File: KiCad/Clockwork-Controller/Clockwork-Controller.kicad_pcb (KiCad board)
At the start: 2 copper layers, 56.4 x 94.2 mm, 97 parts, among them CN2 PJ-307N5, J2 to DIN-6 Male, J3 Pause Button, J4 ICSP, J5 LED-Connector, Q1 AO3400A, Q2 SS8050, Q3 SS8050, Q4 SS8050, SW1 Guide/Follow, SW2 Mode -, SW3 Mode +, SW4 Frame -, SW5 Frame +, U1 ECS-TXO-3225MV-160-TR, U2 AP2210N-3.3TRG1, U3 74HCT14, U4 G3VM-61VY3(TR), U5 MCP4725, U6 LMC6482, U7 ATmega328P-A

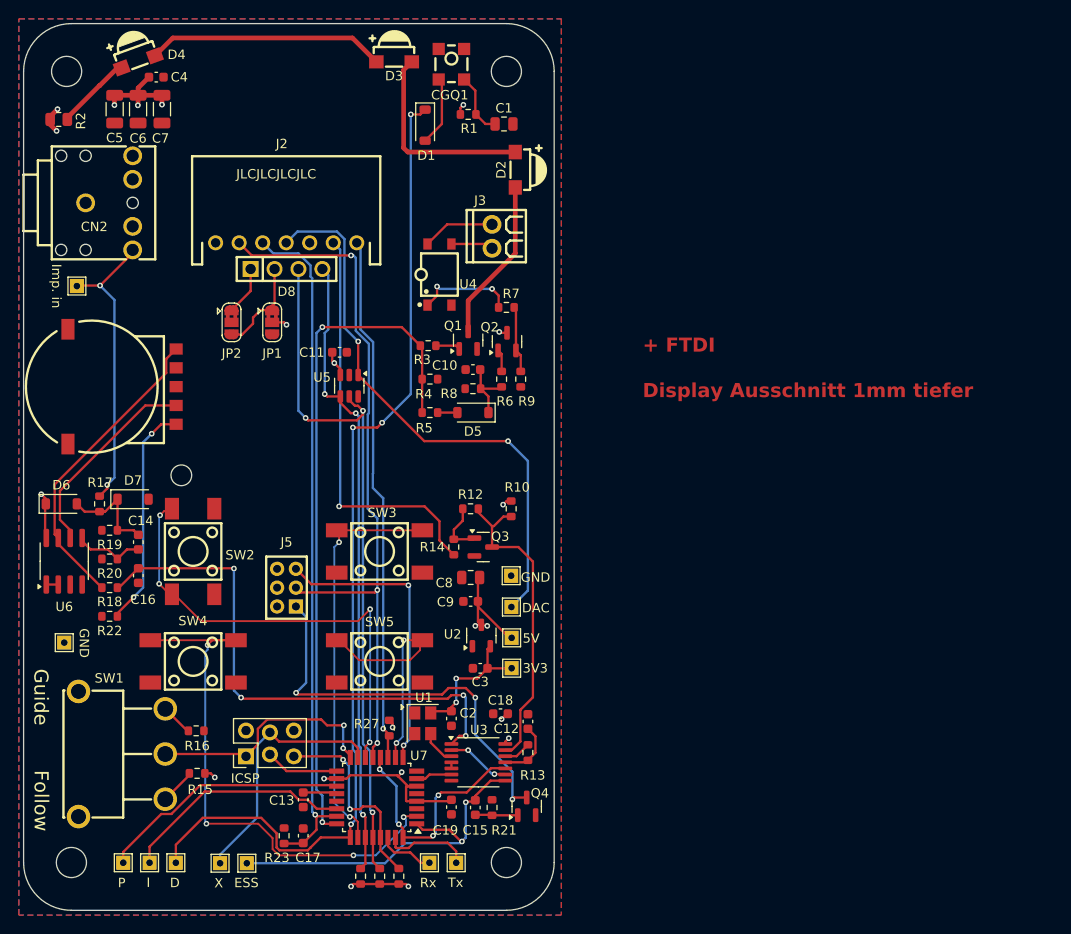
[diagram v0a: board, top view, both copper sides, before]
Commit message: Adding FTDI port
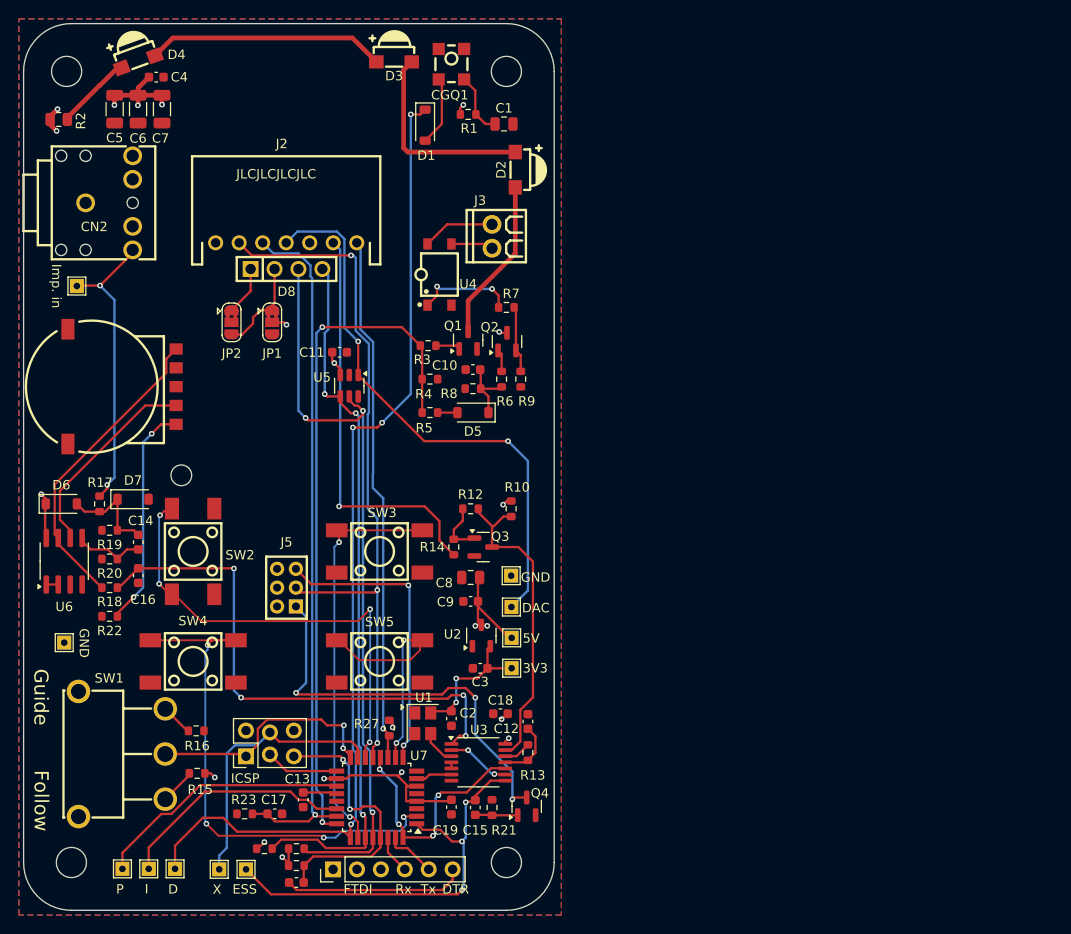
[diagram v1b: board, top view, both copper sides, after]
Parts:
- removed TP12: Rx, TestPoint:TestPoint_THTPad_1.5x1.5mm_Drill0.7mm
- removed TP13: Tx, TestPoint:TestPoint_THTPad_1.5x1.5mm_Drill0.7mm
- added C20: 100n, Capacitor_SMD:C_0603_1608Metric, F.Cu at (67.6, 111.6)
- added J6: FTDI, Connector_PinHeader_2.54mm:PinHeader_1x06_P2.54mm_Vertical, F.Cu at (71.5, 110.2)
- moved R26 10.9 mm to (67.6, 109.8), turned to 0 degrees
- moved R24 10.6 mm to (64.2, 108.0), turned to 180 degrees
- moved R25 9.33 mm to (67.6, 108.0), turned to 0 degrees
- moved R23 4.80 mm to (62.1, 104.3), turned to 180 degrees
- moved C17 3.82 mm to (65.3, 104.3), turned to 0 degrees
- moved TP10 0.66 mm to (62.2, 110.2)
- moved TP6 0.66 mm to (49.1, 110.1)
- moved TP7 0.66 mm to (51.9, 110.1)
- moved TP8 0.66 mm to (59.4, 110.2)
- moved TP11 0.66 mm to (54.7, 110.1)
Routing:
- net /DTR: track 0.00 -> 19.3 mm
- net /SDA: track 67.2 -> 75.5 mm
- net /~{RST}: track 21.5 -> 29.2 mm
- net /INT1: track 39.4 -> 44.9 mm, vias 2 -> 3
- net /SCL: track 74.7 -> 79.9 mm
- net /TX: track 9.36 -> 5.55 mm
- net /Frame-: track 57.7 -> 55.5 mm
- net +5V: track 66.7 -> 64.4 mm
- net /MOSI: track 27.1 -> 29.2 mm
- net /RX: track 6.06 -> 4.13 mm
- net /Proj_ID: track 72.7 -> 74.5 mm
- net /D_POT: track 107.6 -> 106.3 mm
- net /I_POT: track 24.8 -> 25.5 mm
- net /P_POT: track 26.8 -> 27.5 mm
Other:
- board text added: "DTR"
- board text added: "FTDI"
- board text removed: "+ FTDI Display Ausschnitt 1mm tiefer"

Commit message: Label it Rev.B
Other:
- board text added: "Rev.B"
- board text removed: "Rev.A"
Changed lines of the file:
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@@
 		)
 	)
-	(gr_text "Rev.A"
+	(gr_text "Rev.B"
 		(at 71.628 79.756 90)
 		(layer "B.SilkS")

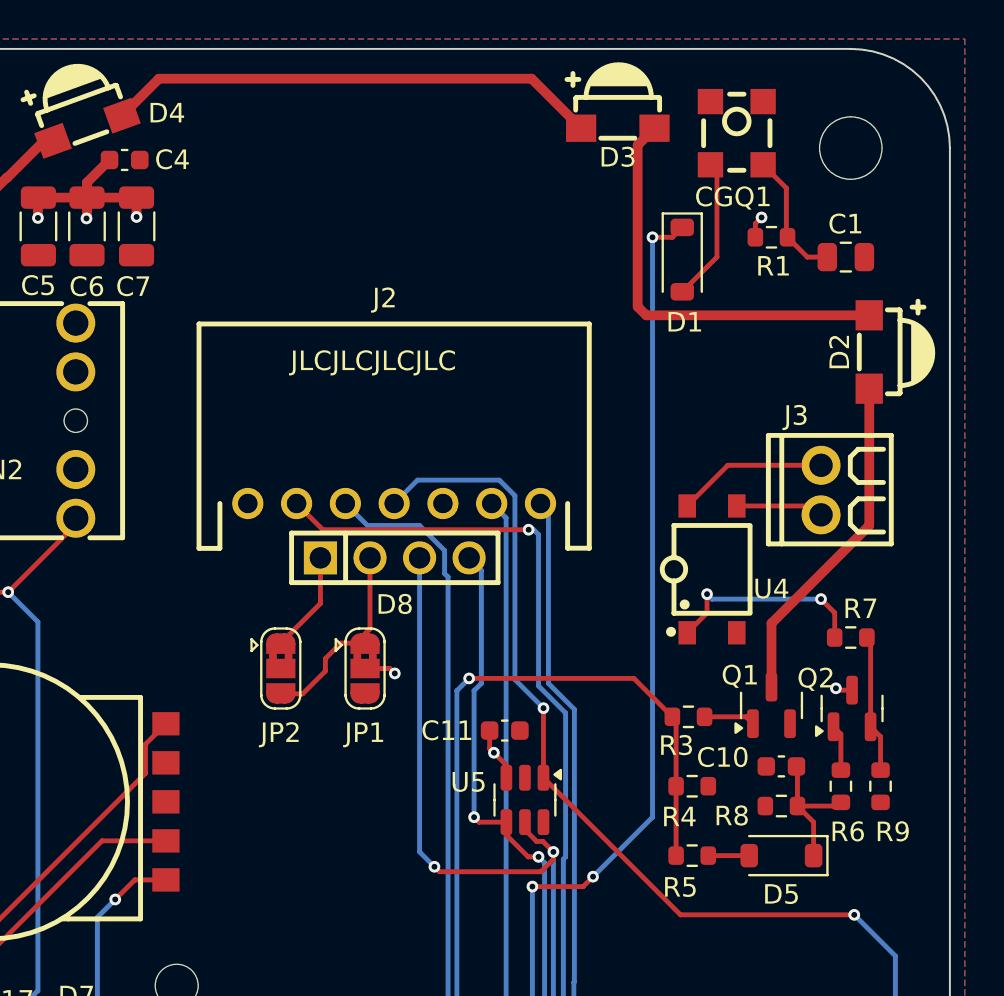
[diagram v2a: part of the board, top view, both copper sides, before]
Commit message: Swapping IR Tx and Rx for better reach
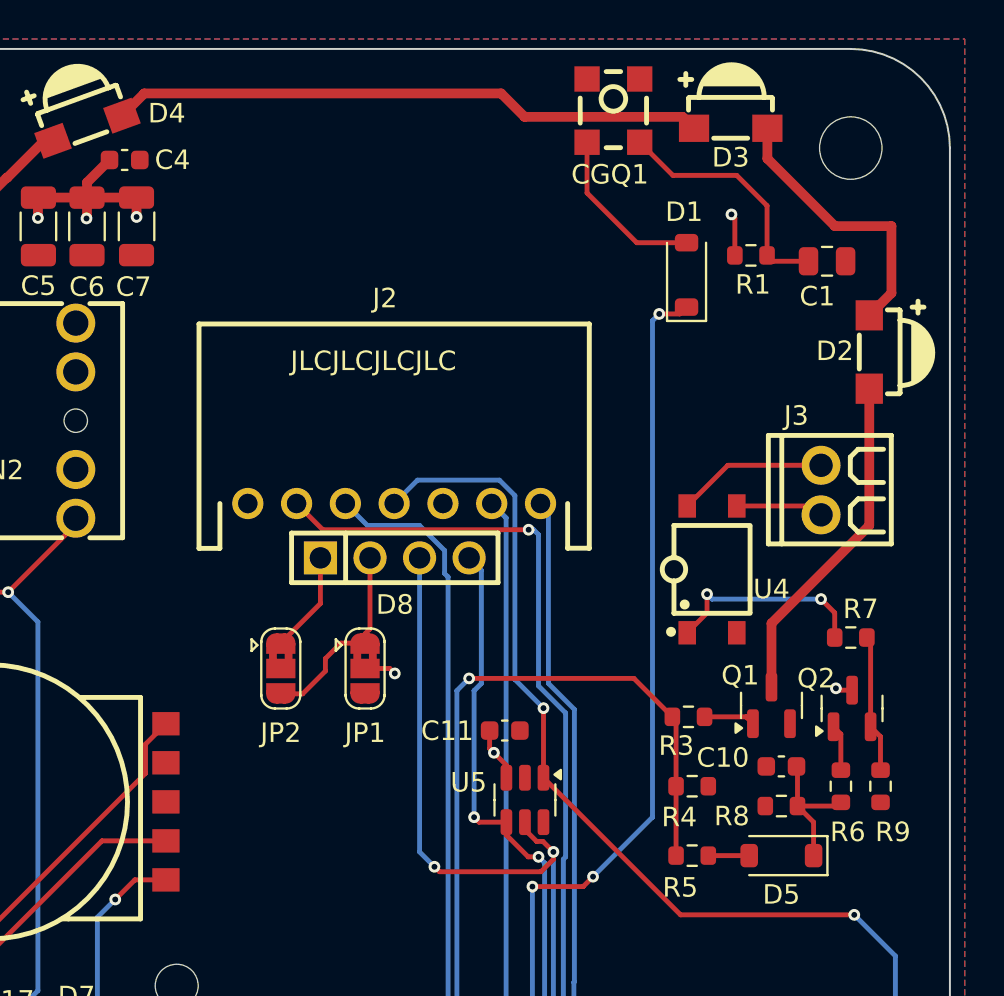
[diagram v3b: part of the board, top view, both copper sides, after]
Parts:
- moved CGQ1 6.43 mm to (77.8, 23.5)
- moved D3 5.78 mm to (83.8, 24.4)
- moved R1 1.40 mm to (84.8, 30.9)
- moved C1 0.99 mm to (88.7, 31.2)
- moved D1 0.82 mm to (81.5, 31.9), turned to 90 degrees
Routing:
- net Net-(D2-A): track 21.6 -> 14.4 mm
- net Net-(CGQ1-VCC): track 6.69 -> 12.7 mm
- net Net-(D3-A): track 25.4 -> 30.5 mm
- net /D_POT: track 106.3 -> 102.3 mm
- net Net-(CGQ1-VOUT): track 7.38 -> 8.76 mm
- net +5V: track 64.4 -> 65.5 mm

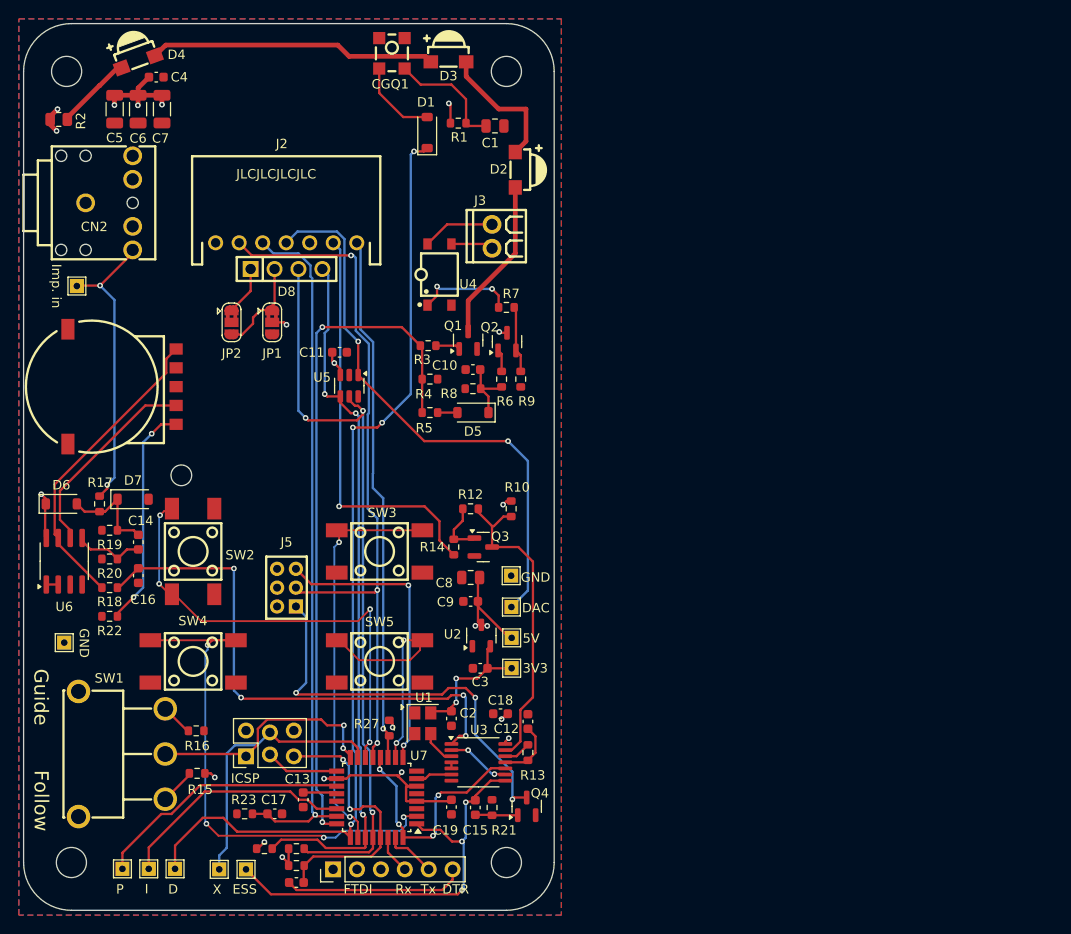
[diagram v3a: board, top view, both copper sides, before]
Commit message: Adjusting LED-Pins on the Controller Side (adding VCC)
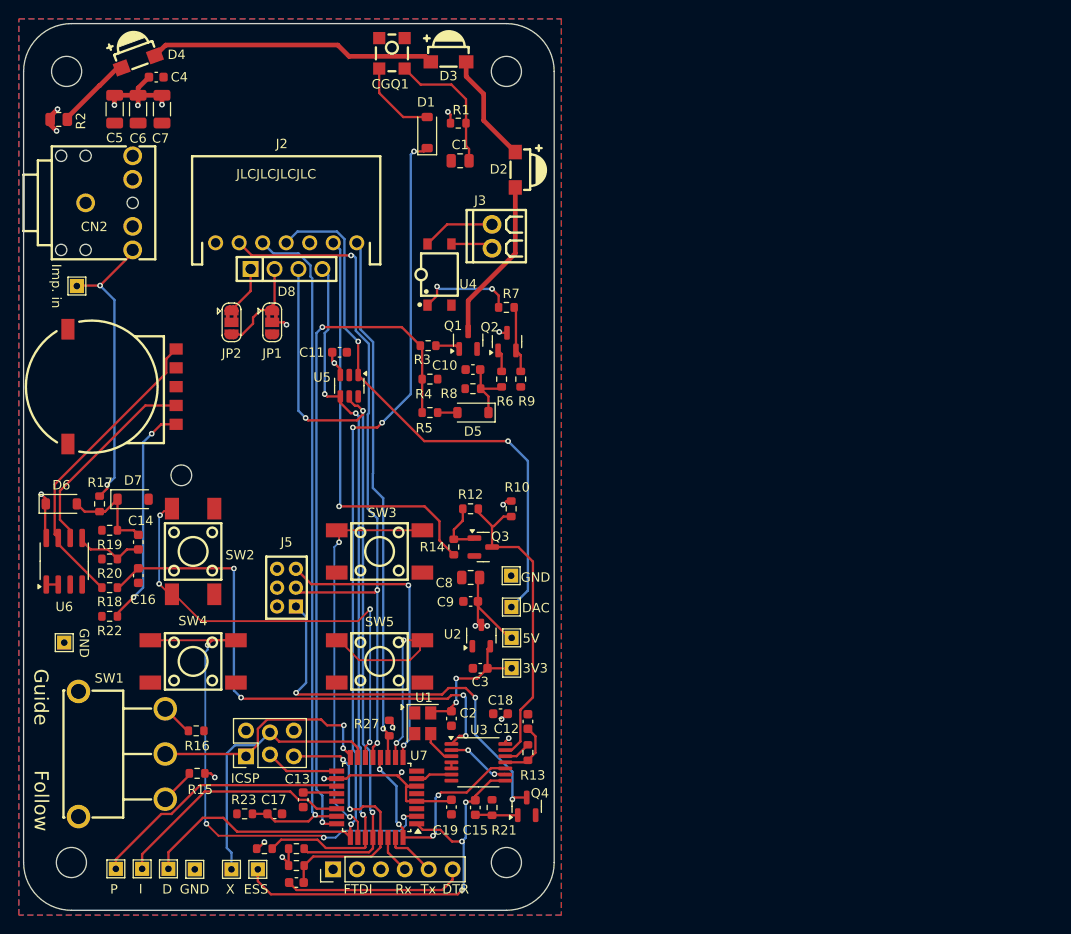
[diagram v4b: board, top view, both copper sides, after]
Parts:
- added TP12: GND, TestPoint:TestPoint_THTPad_1.5x1.5mm_Drill0.7mm, F.Cu at (56.8, 110.2)
- moved C1 5.23 mm to (85.0, 34.9), turned to 180 degrees
- moved TP8 1.30 mm to (60.7, 110.2)
- moved TP10 1.26 mm to (63.5, 110.2)
- moved TP11 0.70 mm to (54.0, 110.1)
- moved TP6 0.70 mm to (48.4, 110.1)
- moved TP7 0.70 mm to (51.2, 110.1)
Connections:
- net /In_Sync-LED renamed /No_Sync-LED
- J5 pad 2: GND -> +5V
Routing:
- net Net-(D2-A): track 14.4 -> 11.7 mm
- net Net-(CGQ1-VCC): track 12.7 -> 14.6 mm
- net +5V: track 65.5 -> 64.6 mm
- net /INT1: track 44.9 -> 44.4 mm

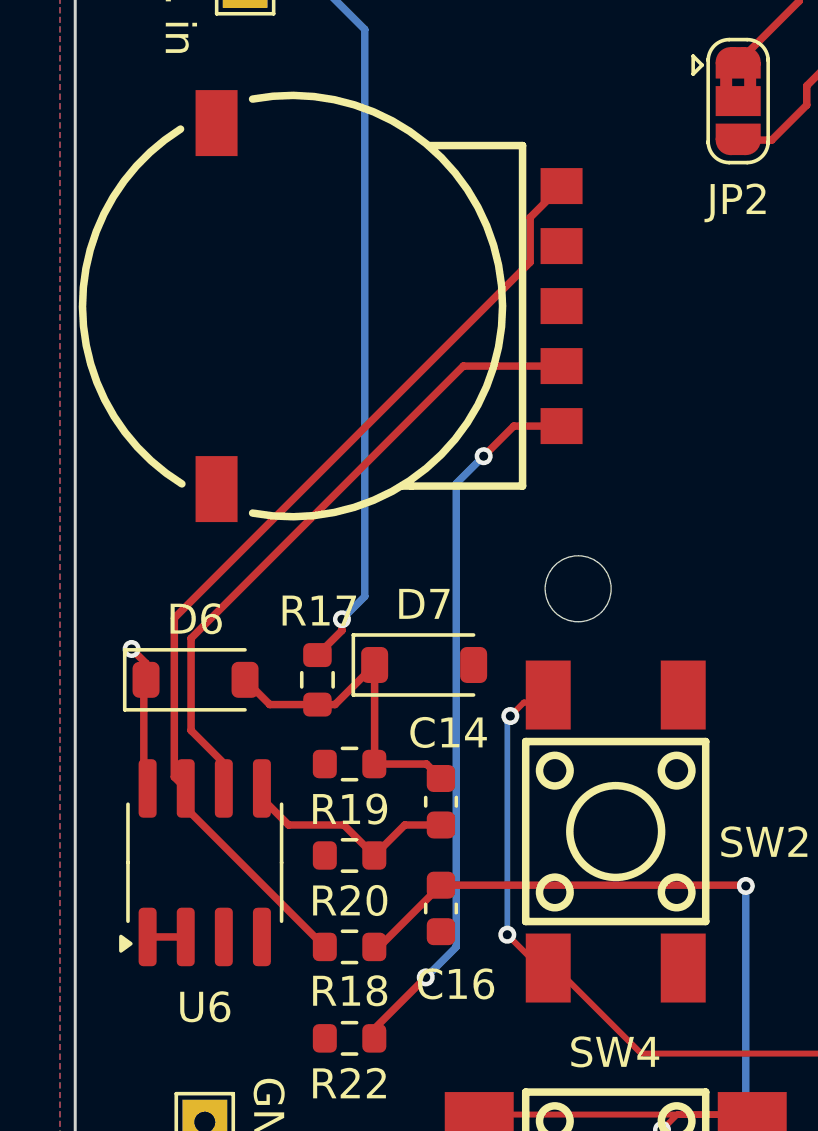
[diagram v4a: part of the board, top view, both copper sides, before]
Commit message: Potentiometer Flip for more intuitive Pulse Amp control
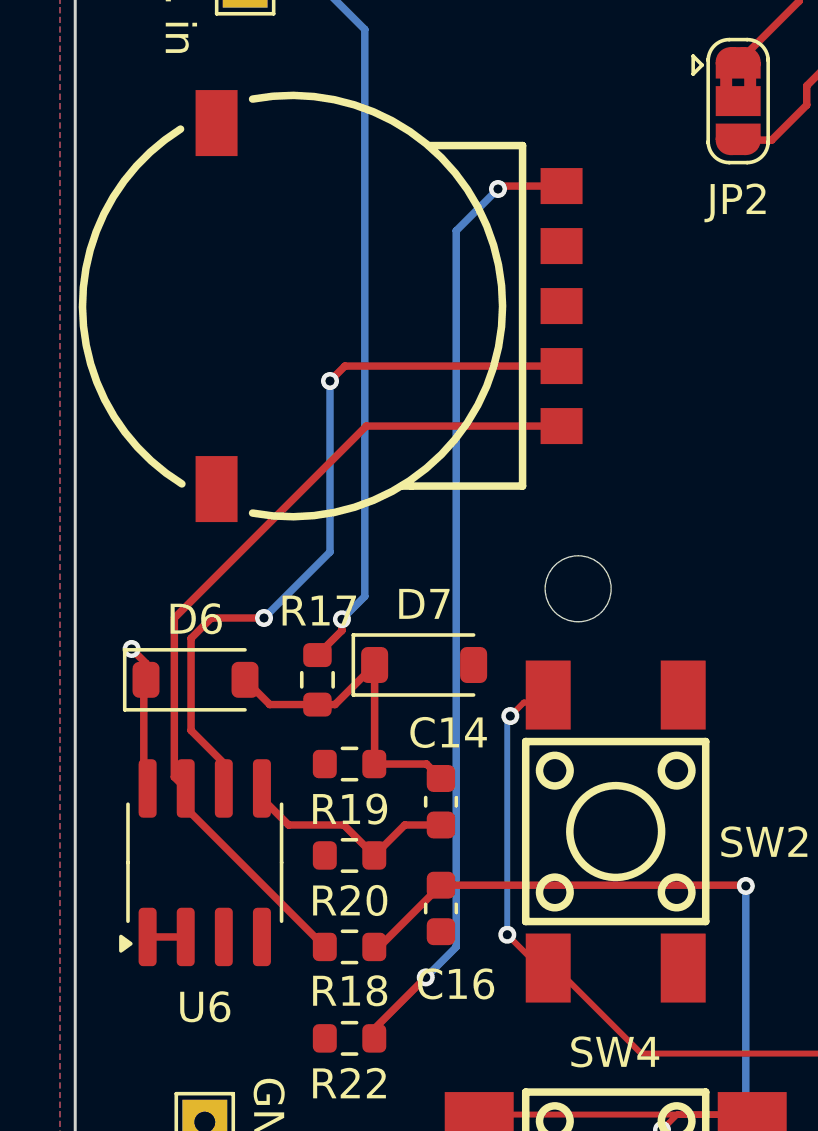
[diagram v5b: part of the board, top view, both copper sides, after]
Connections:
- RV1 pad 1: Net-(R22-Pad1) -> Net-(R18-Pad1)
- RV1 pad 3: Net-(R18-Pad1) -> Net-(R22-Pad1)
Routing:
- net Net-(R22-Pad1): track 23.9 -> 32.2 mm
- net Net-(R18-Pad1): track 32.8 -> 28.6 mm
- net Net-(U6B--): track 21.6 -> 24.9 mm, vias 0 -> 2
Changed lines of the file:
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@@
 			(size 1.4 1.2)
 			(layers "F.Cu" "F.Paste" "F.Mask")
-			(net 56 "Net-(R22-Pad1)")
+			(net 55 "Net-(R18-Pad1)")
 			(pinfunction "1")
 			(pintype "passive")
@@
 			(size 1.4 1.2)
 			(layers "F.Cu" "F.Paste" "F.Mask")
-			(net 55 "Net-(R18-Pad1)")
+			(net 56 "Net-(R22-Pad1)")
 			(pinfunction "3")
 			(pintype "passive")
@@
 	)
 	(segment
-		(start 53.7718 57.440922)
-		(end 53.7718 55.949932)
-		(width 0.25)
-		(layer "F.Cu")
-		(net 55)
-	)
-	(segment
 		(start 42.291 75.628)
 		(end 42.291 74.982)
@@
 	)
 	(segment
-		(start 53.7718 55.949932)
-		(end 54.819132 54.9026)
+		(start 41.91 69.302722)
+		(end 48.310122 62.9026)
 		(width 0.25)
 		(layer "F.Cu")
@@
 	)
 	(segment
-		(start 41.91 69.302722)
-		(end 53.7718 57.440922)
+		(start 48.310122 62.9026)
+		(end 54.819132 62.9026)
 		(width 0.25)
 		(layer "F.Cu")
@@
 	)
 	(segment
-		(start 52.2224 63.9064)
-		(end 53.2262 62.9026)
+		(start 54.819132 54.9026)
+		(end 52.7974 54.9026)
 		(width 0.25)
 		(layer "F.Cu")
@@
 	)
 	(segment
-		(start 50.292 81.28)
-		(end 48.577 82.995)
+		(start 52.7974 54.9026)
+		(end 52.7 55)
 		(width 0.25)
 		(layer "F.Cu")
@@
 	)
 	(segment
-		(start 53.2262 62.9026)
-		(end 54.819132 62.9026)
+		(start 50.292 81.28)
+		(end 48.577 82.995)
 		(width 0.25)
 		(layer "F.Cu")
@@
 	)
 	(via
-		(at 52.2224 63.9064)
+		(at 52.7 55)
 		(size 0.6)
 		(drill 0.3)
@@
 	)
 	(segment
-		(start 51.308 80.264)
-		(end 50.292 81.28)
+		(start 51.308 56.392)
+		(end 51.308 80.264)
 		(width 0.25)
 		(layer "B.Cu")
@@
 	)
 	(segment
-		(start 52.2224 63.9064)
-		(end 51.308 64.8208)
+		(start 52.7 55)
+		(end 51.308 56.392)
 		(width 0.25)
 		(layer "B.Cu")
@@
 	)
 	(segment
-		(start 51.308 64.8208)
-		(end 51.308 80.264)
+		(start 51.308 80.264)
+		(end 50.292 81.28)
 		(width 0.25)
 		(layer "B.Cu")
@@
 	)
 	(segment
-		(start 51.5432 60.9026)
-		(end 42.4688 69.977)
+		(start 44.9 69.3)
+		(end 43.1458 69.3)
 		(width 0.25)
 		(layer "F.Cu")
@@
 	(segment
 		(start 54.819132 60.9026)
-		(end 51.5432 60.9026)
+		(end 47.5974 60.9026)
+		(width 0.25)
+		(layer "F.Cu")
+		(net 57)
+	)
+	(segment
+		(start 47.5974 60.9026)
+		(end 47.1 61.4)
 		(width 0.25)
 		(layer "F.Cu")
@@
 	)
 	(segment
+		(start 43.1458 69.3)
+		(end 42.4688 69.977)
+		(width 0.25)
+		(layer "F.Cu")
+		(net 57)
+	)
+	(segment
 		(start 42.4688 69.977)
 		(end 42.4688 73.0504)
@@
 		(net 57)
 	)
+	(via
+		(at 47.1 61.4)
+		(size 0.6)
+		(drill 0.3)
+		(layers "F.Cu" "B.Cu")
+		(net 57)
+	)
+	(via
+		(at 44.9 69.3)
+		(size 0.6)
+		(drill 0.3)
+		(layers "F.Cu" "B.Cu")
+		(net 57)
+	)
+	(segment
+		(start 47.1 67.1)
+		(end 44.9 69.3)
+		(width 0.25)
+		(layer "B.Cu")
+		(net 57)
+	)
+	(segment
+		(start 47.1 61.4)
+		(end 47.1 67.1)
+		(width 0.25)
+		(layer "B.Cu")
+		(net 57)
+	)
